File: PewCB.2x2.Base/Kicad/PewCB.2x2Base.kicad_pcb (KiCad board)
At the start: 2 copper layers, 40.6 x 38.1 mm, 4 parts

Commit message: fixes
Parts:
- moved H** 2.54 mm to (15.2, 15.2)
- moved H** 2.54 mm to (15.2, -15.2)
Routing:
- net GND: vias 78 -> 76
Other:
- board size 40.6 x 38.1 mm -> 38.1 x 38.1 mm

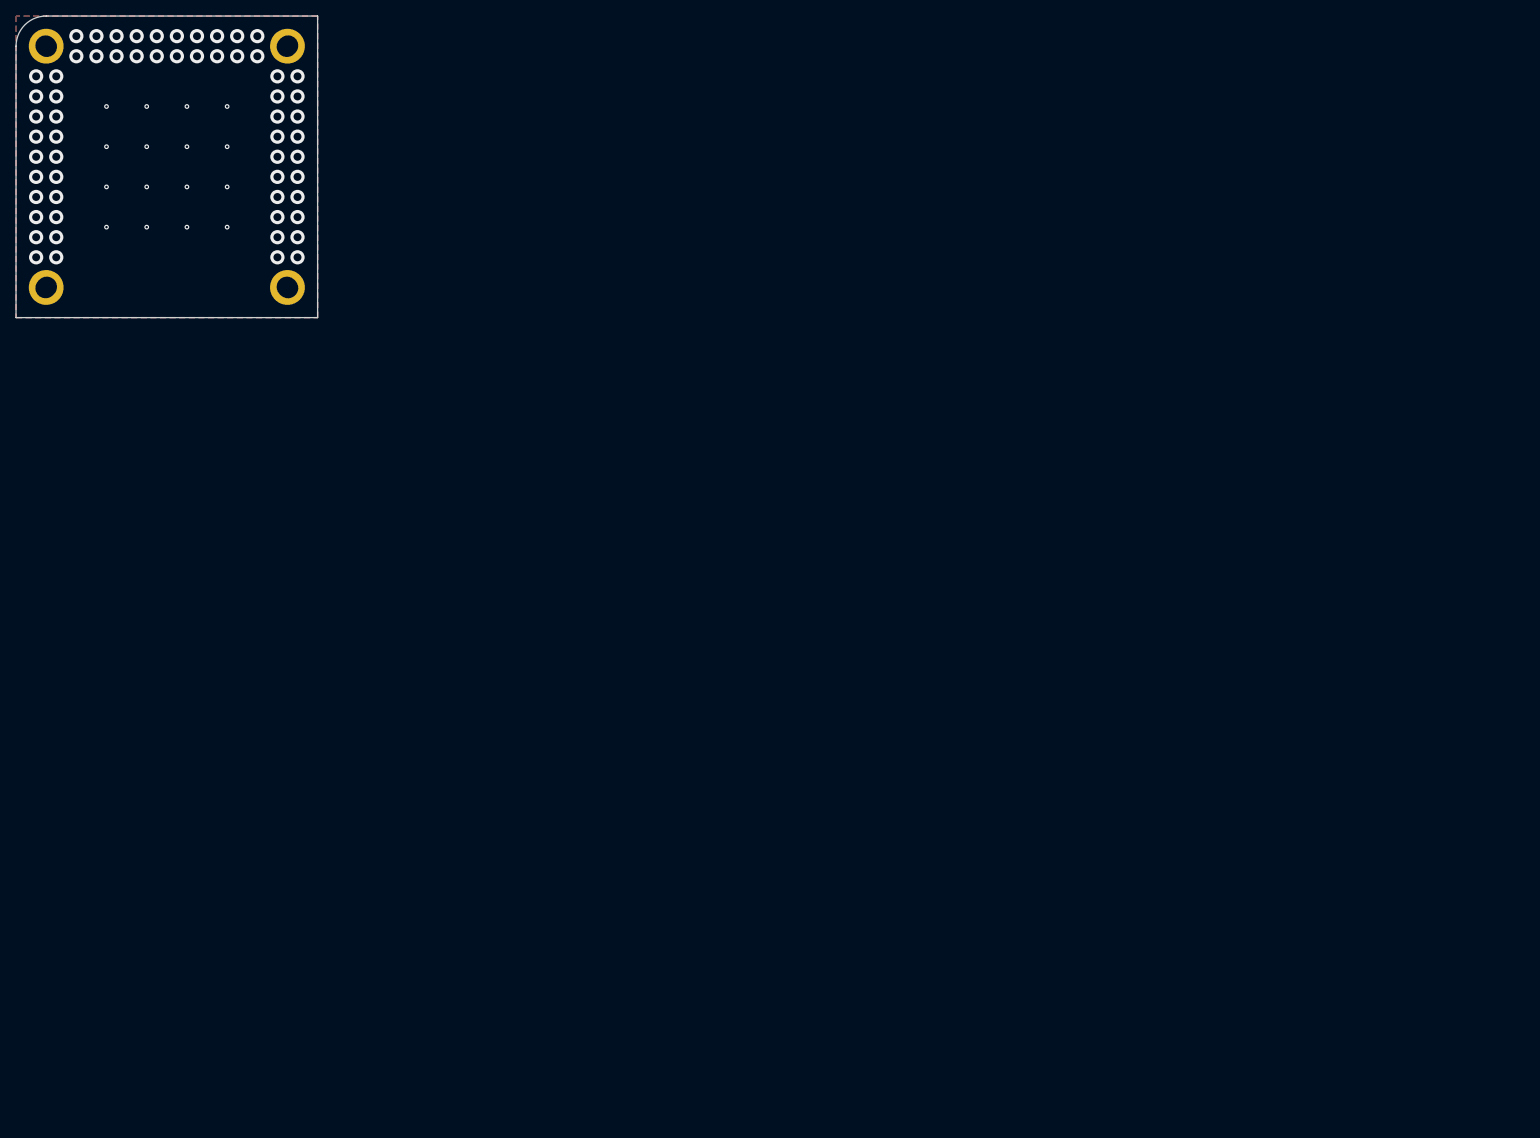
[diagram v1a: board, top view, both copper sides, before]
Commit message: fixed kicad board origins
removed empty page layouts
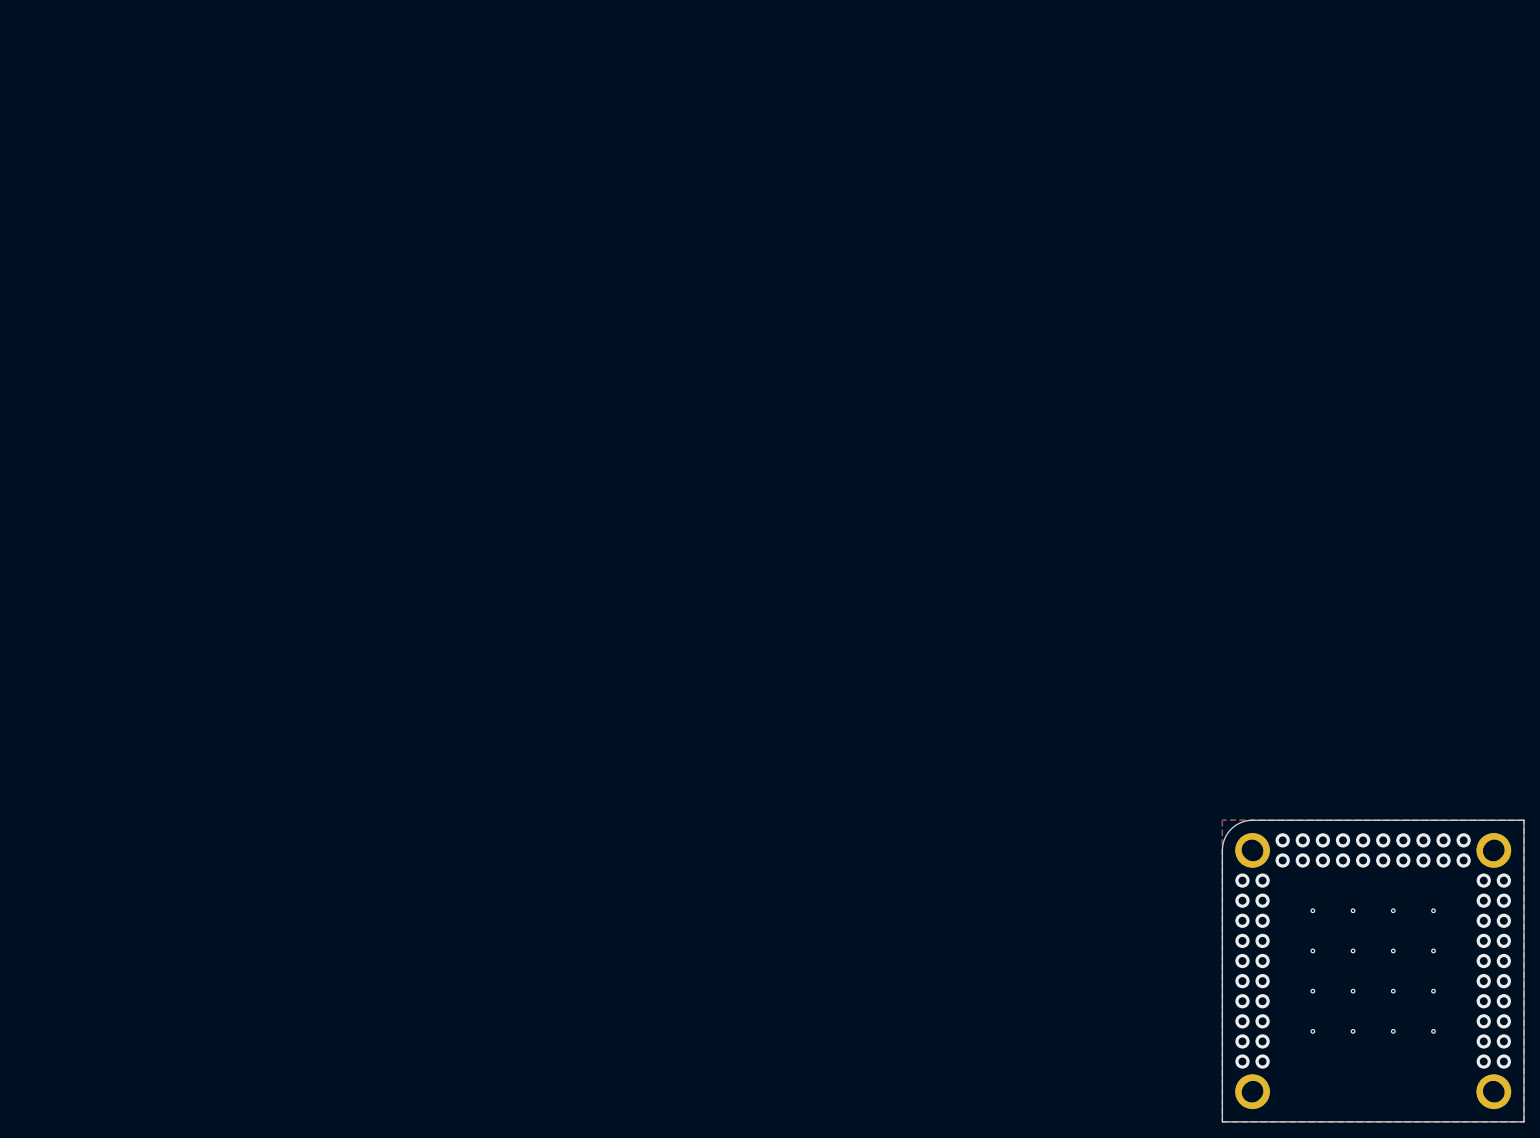
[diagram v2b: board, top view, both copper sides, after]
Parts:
- moved H** 183.2 mm to (137.2, 86.4)
- moved H** 183.2 mm to (137.2, 116.8)
- moved H** 183.2 mm to (167.6, 116.8)
- moved H** 183.2 mm to (167.6, 86.4)
